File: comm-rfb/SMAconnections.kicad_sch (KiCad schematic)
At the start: 4 parts

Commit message: added test connectors and programming interfaces
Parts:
- J?: footprint (none) -> Connector_Coaxial:SMA_Amphenol_132134-10_Vertical
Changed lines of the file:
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@@
       (effects (font (size 1.27 1.27)) (justify left))
     )
-    (property "Footprint" "" (id 2) (at 55.88 44.45 0)
+    (property "Footprint" "Connector_Coaxial:SMA_Amphenol_132134-10_Vertical" (id 2) (at 55.88 44.45 0)
       (effects (font (size 1.27 1.27)) hide)
     )

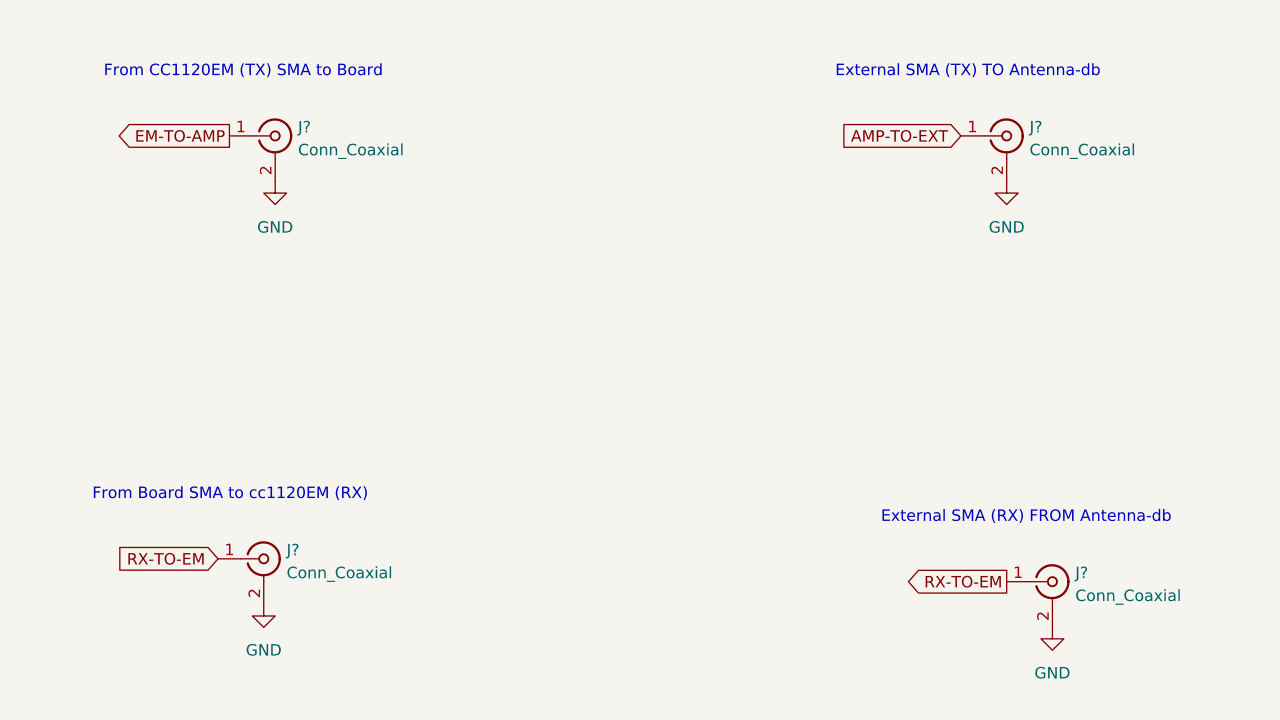
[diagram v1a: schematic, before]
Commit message: comm-rfb: reformat main schematic page
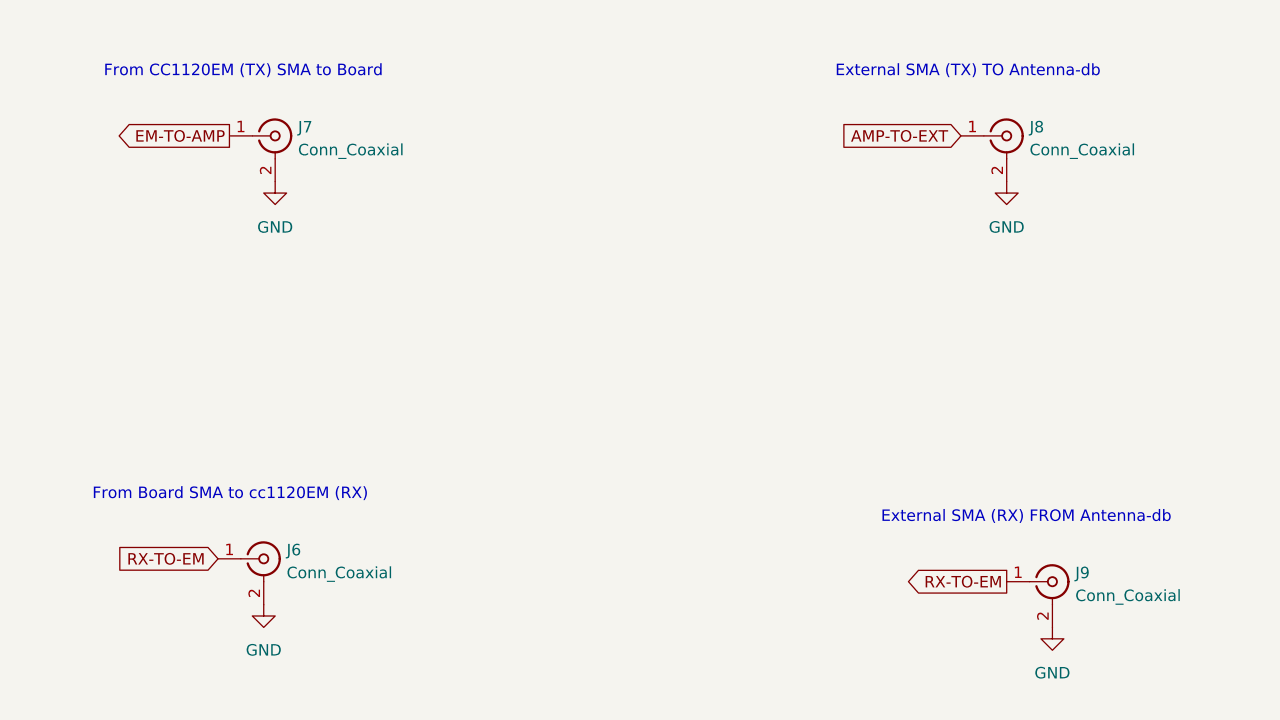
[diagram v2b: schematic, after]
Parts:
- gave numbers to parts that had none: 4
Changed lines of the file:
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@@
   (symbol (lib_id "power:GND") (at 55.88 49.53 0) (unit 1)
     (in_bom yes) (on_board yes) (fields_autoplaced)
-    (property "Reference" "#PWR?" (id 0) (at 55.88 55.88 0)
+    (property "Reference" "#PWR06" (id 0) (at 55.88 55.88 0)
       (effects (font (size 1.27 1.27)) hide)
     )
@@
   (symbol (lib_id "Connector:Conn_Coaxial") (at 55.88 44.45 0) (unit 1)
     (in_bom yes) (on_board yes) (fields_autoplaced)
-    (property "Reference" "J?" (id 0) (at 58.42 43.4731 0)
+    (property "Reference" "J7" (id 0) (at 58.42 43.4731 0)
       (effects (font (size 1.27 1.27)) (justify left))
     )
@@
   (symbol (lib_id "Connector:Conn_Coaxial") (at 142.24 93.98 0) (unit 1)
     (in_bom yes) (on_board yes) (fields_autoplaced)
-    (property "Reference" "J?" (id 0) (at 144.78 93.0031 0)
+    (property "Reference" "J9" (id 0) (at 144.78 93.0031 0)
       (effects (font (size 1.27 1.27)) (justify left))
     )
@@
   (symbol (lib_id "Connector:Conn_Coaxial") (at 54.61 91.44 0) (unit 1)
     (in_bom yes) (on_board yes) (fields_autoplaced)
-    (property "Reference" "J?" (id 0) (at 57.15 90.4631 0)
+    (property "Reference" "J6" (id 0) (at 57.15 90.4631 0)
       (effects (font (size 1.27 1.27)) (justify left))
     )
@@
   (symbol (lib_id "power:GND") (at 142.24 99.06 0) (unit 1)
     (in_bom yes) (on_board yes) (fields_autoplaced)
-    (property "Reference" "#PWR?" (id 0) (at 142.24 105.41 0)
+    (property "Reference" "#PWR08" (id 0) (at 142.24 105.41 0)
       (effects (font (size 1.27 1.27)) hide)
     )
@@
   (symbol (lib_id "power:GND") (at 54.61 96.52 0) (unit 1)
     (in_bom yes) (on_board yes) (fields_autoplaced)
-    (property "Reference" "#PWR?" (id 0) (at 54.61 102.87 0)
+    (property "Reference" "#PWR05" (id 0) (at 54.61 102.87 0)
       (effects (font (size 1.27 1.27)) hide)
     )
@@
   (symbol (lib_id "power:GND") (at 137.16 49.53 0) (unit 1)
     (in_bom yes) (on_board yes) (fields_autoplaced)
-    (property "Reference" "#PWR?" (id 0) (at 137.16 55.88 0)
+    (property "Reference" "#PWR07" (id 0) (at 137.16 55.88 0)
       (effects (font (size 1.27 1.27)) hide)
     )
@@
   (symbol (lib_id "Connector:Conn_Coaxial") (at 137.16 44.45 0) (unit 1)
     (in_bom yes) (on_board yes) (fields_autoplaced)
-    (property "Reference" "J?" (id 0) (at 139.7 43.4731 0)
+    (property "Reference" "J8" (id 0) (at 139.7 43.4731 0)
       (effects (font (size 1.27 1.27)) (justify left))
     )

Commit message: comm-rfb: reduce number of sheets in schematic
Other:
- note added: "Downlink (Tx) RF System"
- note added: "Uplink (Rx) RF System"
- moved on the sheet: J8, J9
